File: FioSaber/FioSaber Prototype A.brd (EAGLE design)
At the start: 25.4 x 45.3 mm, 19 parts, among them P1 WIICHUCK, T1 2N2222

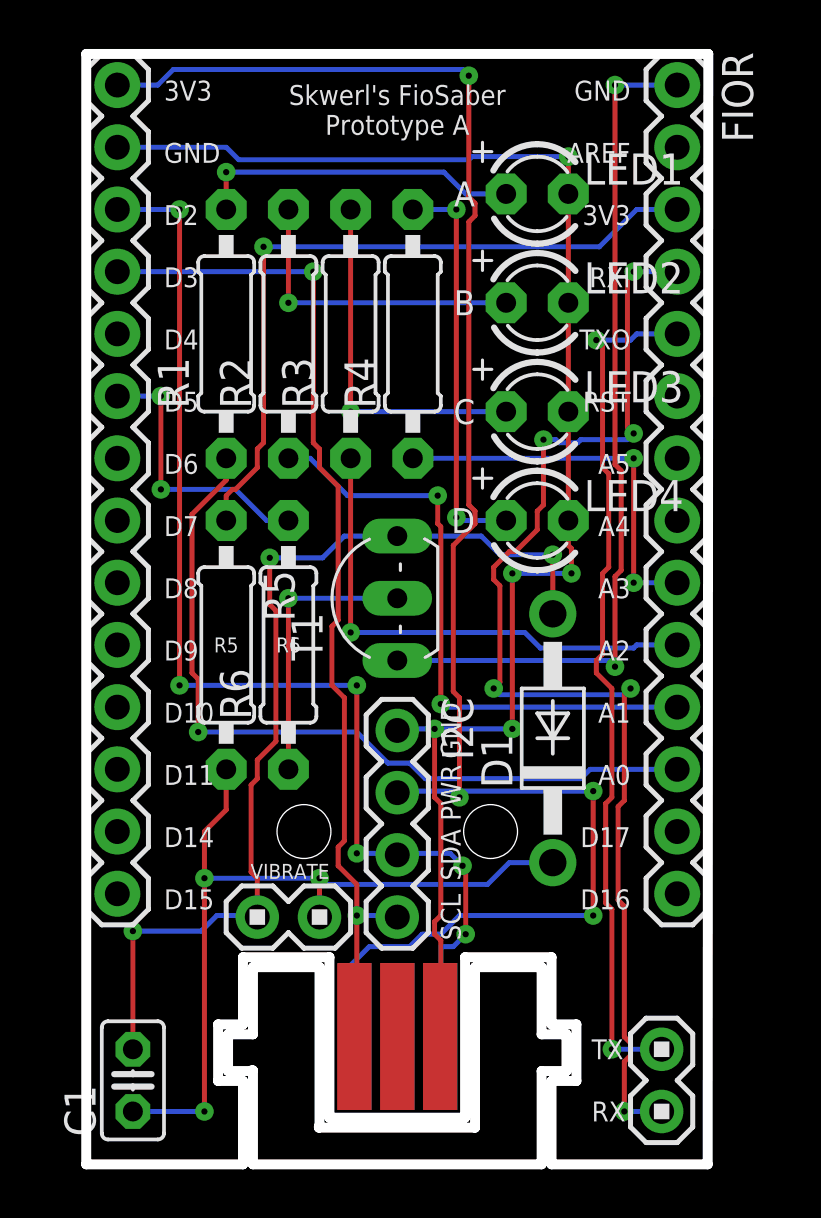
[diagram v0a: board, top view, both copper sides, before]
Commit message: fixed vibe motor circuit
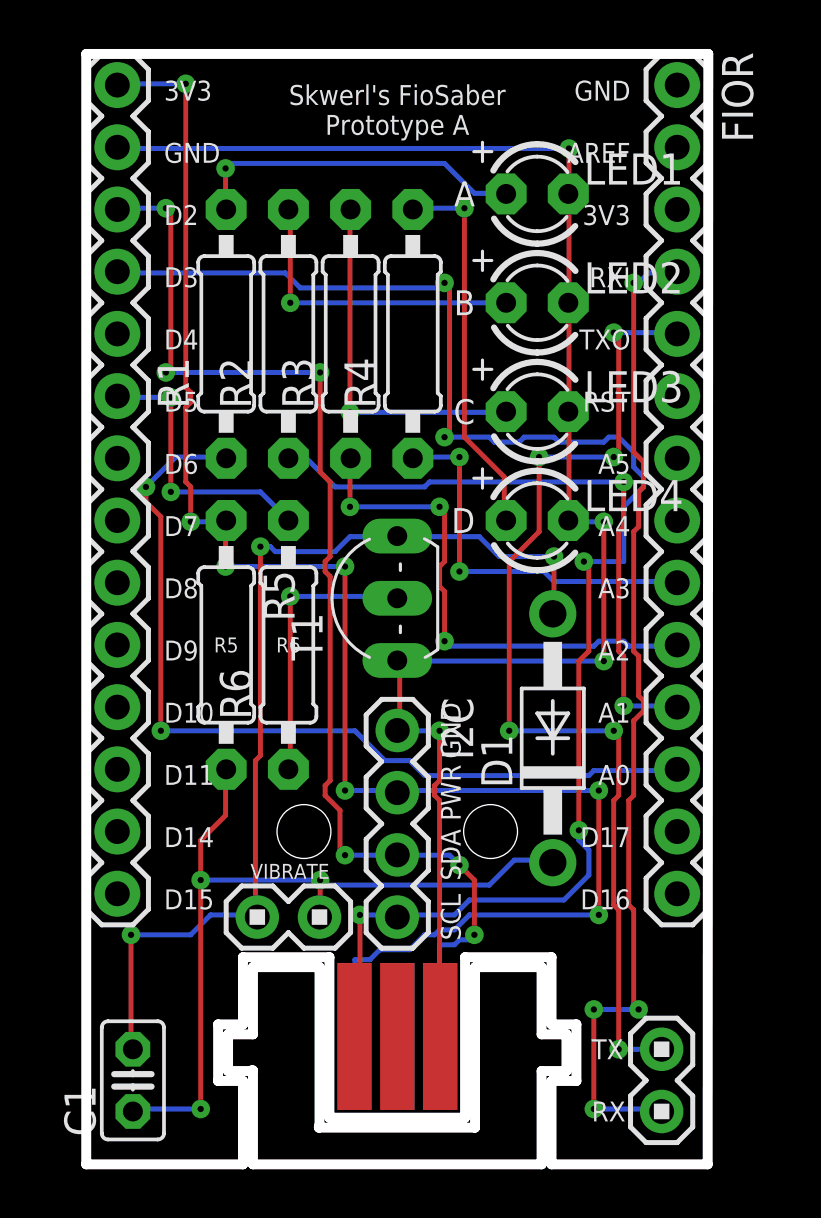
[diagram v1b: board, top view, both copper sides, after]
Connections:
- removed net N$17: FIOR.1, T1.E
- removed net N$2: FIOR.3, R5.1
- net N$1: now also R5.1
- net N$13: now also T1.E
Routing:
- net N$17: track 35.5 -> 0.00 mm, vias 2 -> 0
- net N$2: track 29.4 -> 0.00 mm, vias 1 -> 0
- net N$4: track 42.2 -> 63.4 mm, vias 2 -> 5
- net N$14: track 49.0 -> 41.2 mm, vias 6 -> 4
- net N$15: track 35.3 -> 41.9 mm, vias 2 -> 6
- net N$1: track 72.4 -> 67.7 mm, vias 4 -> 7
- net N$13: track 62.2 -> 66.6 mm, vias 5 -> 4
- net N$5: track 32.4 -> 36.0 mm, vias 1 -> 2
- net N$12: track 16.4 -> 15.6 mm, vias 2 -> 1
- net N$6: track 25.0 -> 25.8 mm
- net N$3: track 48.4 -> 48.9 mm
- net N$7: track 20.8 -> 21.1 mm, vias 1 -> 3
